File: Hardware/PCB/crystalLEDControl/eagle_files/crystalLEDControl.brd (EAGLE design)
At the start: 35 x 35 mm, 6 parts

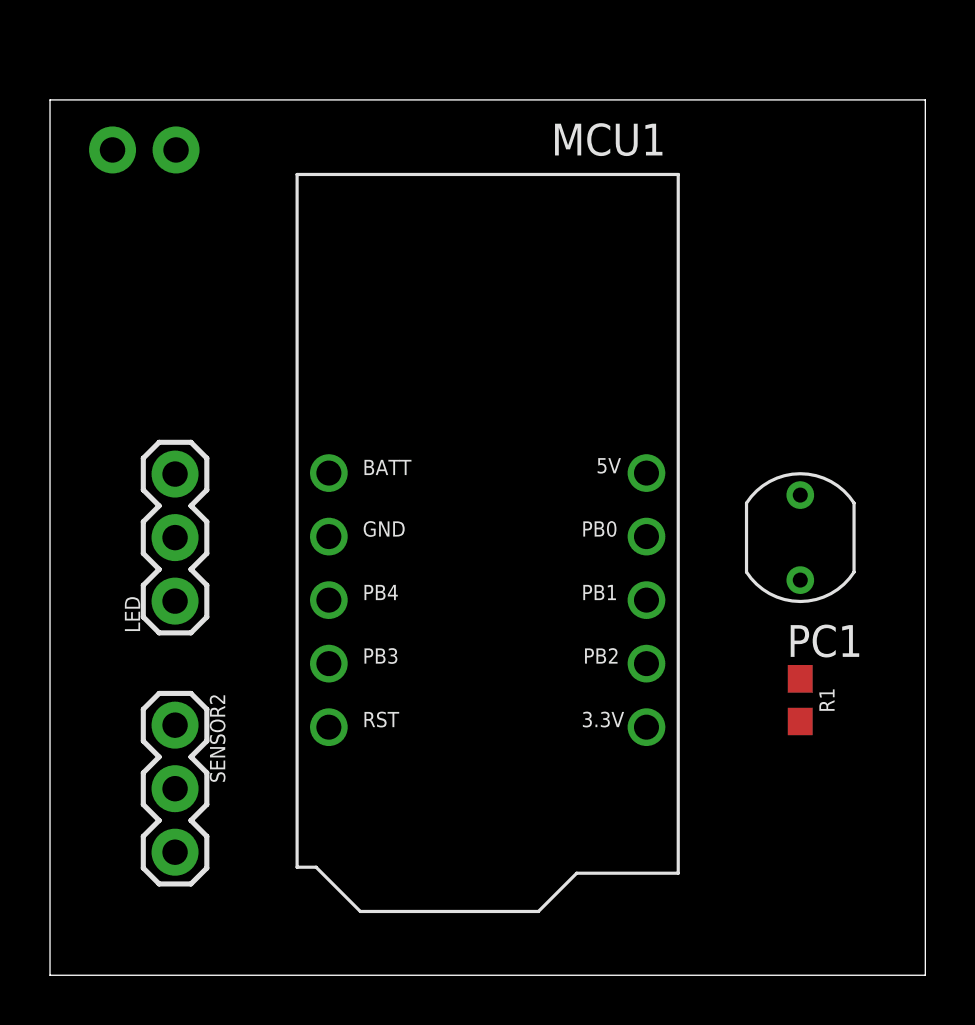
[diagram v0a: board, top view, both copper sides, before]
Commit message: Routing complete. Pin labels as well.
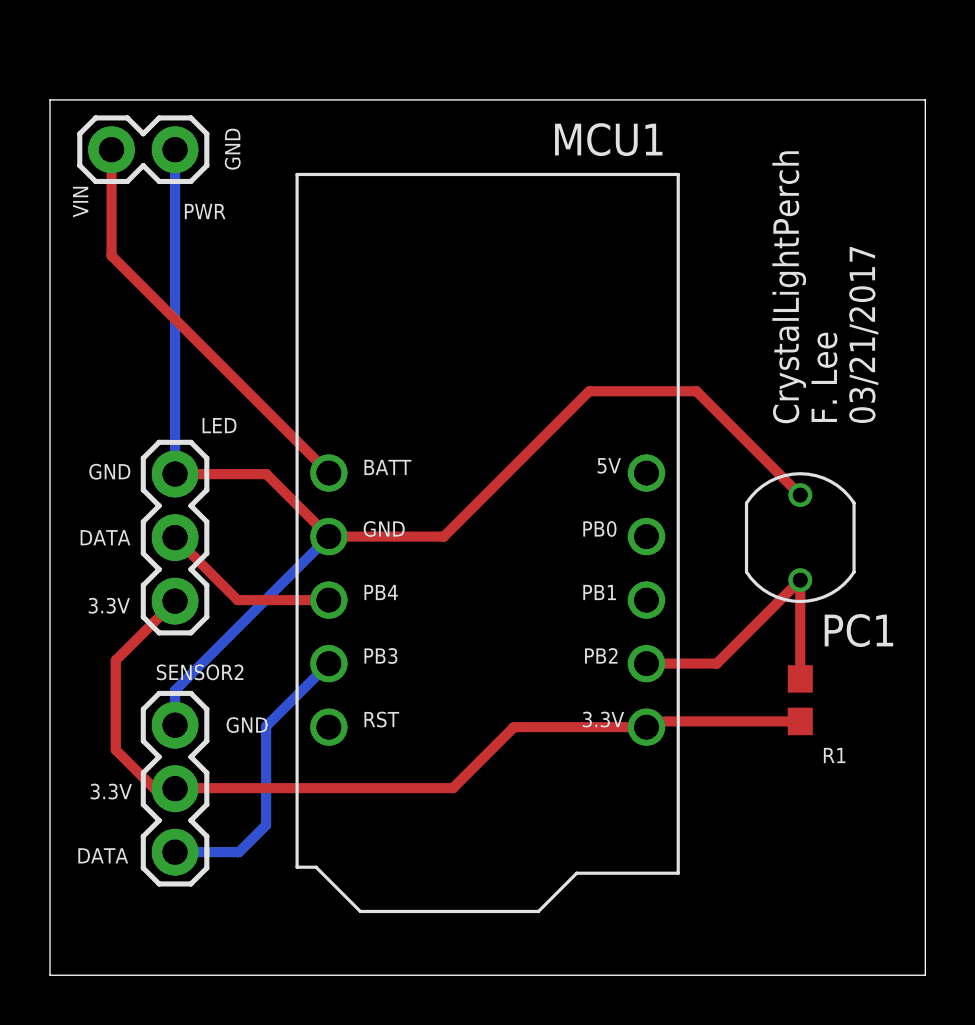
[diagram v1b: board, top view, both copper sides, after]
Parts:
- moved PWR 2.50 mm to (5.00, 33.0), flipped to the top
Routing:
- net GND: track 0.00 -> 53.2 mm
- net 3.3V: track 0.00 -> 36.1 mm
- net VIN: track 0.00 -> 16.5 mm
- net SENSOR_EXP_IN: track 0.00 -> 11.6 mm
- net LIGHT_SENSOR_IN: track 0.00 -> 11.5 mm
- net LED_DATA: track 0.00 -> 7.19 mm
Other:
- board text added: "3.3V"
- board text added: "CrystalLightPerch F. Lee 03/21/2017"
- board text added: "DATA"
- board text added: "GND"
- board text added: "VIN"
